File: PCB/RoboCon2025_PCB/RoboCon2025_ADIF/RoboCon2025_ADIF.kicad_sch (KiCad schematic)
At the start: 37 parts, among them J1 Conn_01x05, J2 1x9, J3 Conn_01x09, J4 S2B-XH-A, J5 Micro_SD_Card_Det_Hirose_DM3AT, J6 S3B-XH-A, J7 S2B-XH-A, J8 S2B-XH-A, J9 S3B-XH-A, U1 PCM5102A, U2 MCP23017_SO

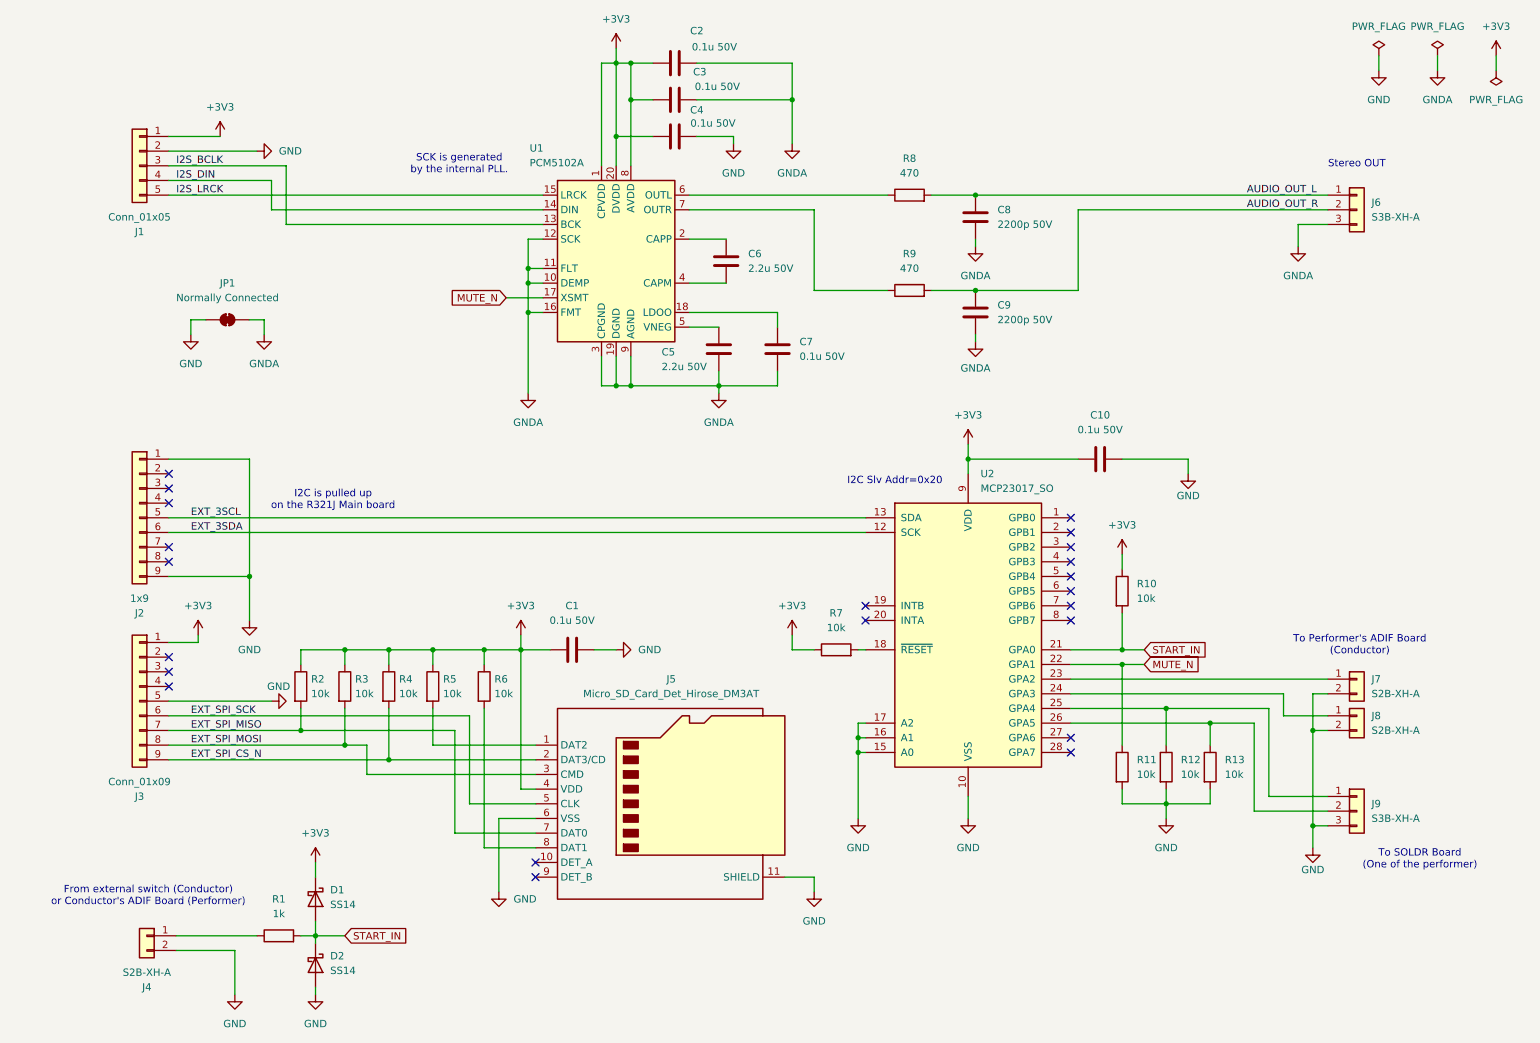
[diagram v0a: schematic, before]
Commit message: [PCB] add: ADIF schematic and layout
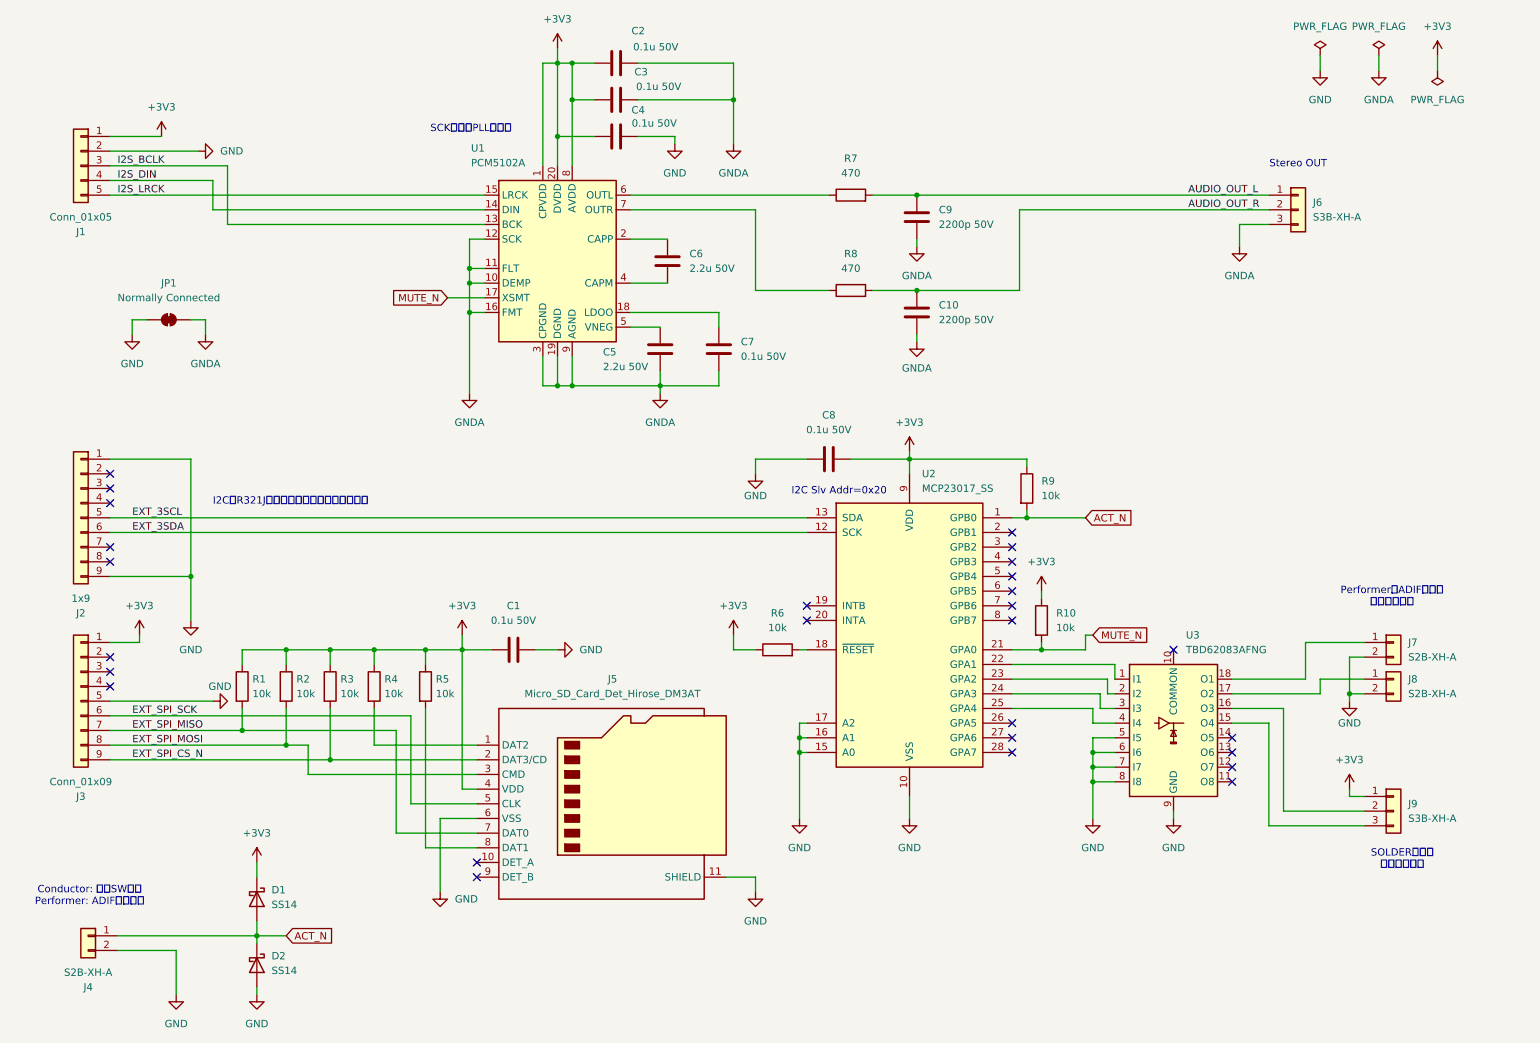
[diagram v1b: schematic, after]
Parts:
- removed R1: 1k, Resistor_SMD:R_0603_1608Metric_Pad0.98x0.95mm_HandSolder, symbol Device:R
- removed R11, R12, R13: 10k, Resistor_SMD:R_0603_1608Metric_Pad0.98x0.95mm_HandSolder, symbol Device:R
- added R10: 10k, Resistor_SMD:R_0603_1608Metric_Pad0.98x0.95mm_HandSolder, symbol Device:R
- added U3: TBD62083AFNG, RoboCon2025_ADIF:TBD62083A_SSOP-18_4.4x6.5mm_P0.65mm, symbol RoboCon2025_ADIF:TBD62083A
- U1: footprint Package_SO:TSSOP-20_4.4x6.5mm_P0.65mm -> Package_SO:Texas_PW0020A_TSSOP-20_4.4x6.5mm_P0.65mm
- U2: value MCP23017_SO -> MCP23017_SS; footprint Package_SO:SOIC-28W_7.5x17.9mm_P1.27mm -> Package_SO:SSOP-28_5.3x10.2mm_P0.65mm
- renumbered C9 to C10, C10 to C8, C8 to C9, R2 to R1, R3 to R2, R4 to R3, R5 to R4, R6 to R5, R7 to R6, R8 to R7, R9 to R8, R10 to R9
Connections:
- net +3V3: now also C8.2, J9.1 (Pin_1), R10.1; no longer C8.1
- net GND: now also C8.1, U3.5 (I5), U3.6 (I6), U3.7 (I7), U3.8 (I8), U3.9 (GND); no longer C8.2, J9.3 (Pin_3)
- net MUTE_N: now also U2.21 (GPA0), R10.2; no longer U2.22 (GPA1)
- net ACT_N: now reaches J4.1 (Pin_1)
- net ACT_N: now also D1.2 (A), D2.1 (K), R9.2, U2.1 (GPB0)
- net at U2.26 (GPA5): no longer J9.2 (Pin_2)
- net at U2.23 (GPA2): now also U3.2 (I2); no longer J7.1 (Pin_1)
- net at U2.24 (GPA3): now also U3.3 (I3); no longer J8.1 (Pin_1)
- net at U2.25 (GPA4): now also U3.4 (I4); no longer J9.1 (Pin_1)
- removed net START_IN: D1.2 (A), D2.1 (K), R9.2, U2.21 (GPA0)
- new net: U2.22 (GPA1), U3.1 (I1)
- new net: J9.2 (Pin_2), U3.16 (O3)
- new net: J9.3 (Pin_3), U3.15 (O4)
- new net: J8.1 (Pin_1), U3.17 (O2)
- new net: J7.1 (Pin_1), U3.18 (O1)
- no-connect marks 22 -> 27
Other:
- note added: "Conductor: 外部SWから Performer: ADIF基板から"
- note added: "I2CはR321Jメインボードでプルアップ済み"
- note added: "PerformerのADIF基板へ 電流吸い込み"
- note added: "SCKは内蔵PLLで生成"
- note added: "SOLDER基板へ 電流吸い込み"
- note removed: "From external switch (Conductor) or Conductor's ADIF Board (Performer)"
- note removed: "I2C is pulled up on the R321J Main board"
- note removed: "SCK is generated by the internal PLL."
- note removed: "To Performer's ADIF Board (Conductor)"
- note removed: "To SOLDR Board (One of the performer)"
- moved on the sheet: C1, C10, C2, C3, C4, C5, C6, C7, C8, C9, D1, D2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

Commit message: ADIF 編集
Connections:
- net AUDIO_OUT_L: now also J6.2 (Pin_2); no longer J6.1 (Pin_1)
- net AUDIO_OUT_R: now also J6.3 (Pin_3); no longer J6.2 (Pin_2)
- net GNDA: now also J6.1 (Pin_1); no longer J6.3 (Pin_3)
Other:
- moved on the sheet: J6
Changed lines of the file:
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@@
 	(wire
 		(pts
+			(xy 236.22 40.64) (xy 236.22 43.18)
+		)
+		(stroke
+			(width 0)
+			(type default)
+		)
+	)
+	(wire
+		(pts
 			(xy 114.3 22.86) (xy 114.3 35.56)
 		)
@@
 	(wire
 		(pts
-			(xy 176.53 45.72) (xy 237.49 45.72)
+			(xy 176.53 45.72) (xy 236.22 45.72)
 		)
 		(stroke
@@
 	(wire
 		(pts
-			(xy 194.31 48.26) (xy 237.49 48.26)
+			(xy 194.31 48.26) (xy 236.22 48.26)
 		)
 		(stroke
@@
 	(wire
 		(pts
-			(xy 232.41 50.8) (xy 232.41 54.61)
-		)
-		(stroke
-			(width 0)
-			(type default)
-		)
-	)
-	(wire
-		(pts
 			(xy 127 68.58) (xy 132.08 68.58)
 		)
@@
 	(wire
 		(pts
+			(xy 233.68 40.64) (xy 236.22 40.64)
+		)
+		(stroke
+			(width 0)
+			(type default)
+		)
+	)
+	(wire
+		(pts
 			(xy 194.31 48.26) (xy 194.31 62.23)
 		)
@@
 	(wire
 		(pts
-			(xy 232.41 50.8) (xy 237.49 50.8)
-		)
-		(stroke
-			(width 0)
-			(type default)
-		)
-	)
-	(wire
-		(pts
 			(xy 41.91 123.19) (xy 36.83 123.19)
 		)
@@
 	(symbol
 		(lib_id "power:GNDA")
-		(at 232.41 54.61 0)
+		(at 233.68 40.64 270)
 		(unit 1)
 		(exclude_from_sim no)
@@
 		(fields_autoplaced yes)
 		(property "Reference" "#PWR030"
-			(at 232.41 60.96 0)
+			(at 227.33 40.64 0)
 			(effects
 				(font
@@
 		)
 		(property "Value" "GNDA"
-			(at 232.41 59.69 0)
+			(at 232.41 36.83 90)
 			(effects
 				(font
@@
 		)
 		(property "Footprint" ""
-			(at 232.41 54.61 0)
+			(at 233.68 40.64 0)
 			(effects
 				(font
@@
 		)
 		(property "Datasheet" ""
-			(at 232.41 54.61 0)
+			(at 233.68 40.64 0)
 			(effects
 				(font
@@
 		)
 		(property "Description" "Power symbol creates a global label with name \"GNDA\" , analog ground"
-			(at 232.41 54.61 0)
+			(at 233.68 40.64 0)
 			(effects
 				(font
@@
 	(symbol
 		(lib_id "Connector_Generic:Conn_01x03")
-		(at 242.57 48.26 0)
+		(at 241.3 45.72 0)
 		(unit 1)
 		(exclude_from_sim no)
@@
 		(fields_autoplaced yes)
 		(property "Reference" "J6"
-			(at 245.11 46.9899 0)
+			(at 243.84 44.4499 0)
 			(effects
 				(font
@@
 		)
 		(property "Value" "S3B-XH-A"
-			(at 245.11 49.5299 0)
+			(at 243.84 46.9899 0)
 			(effects
 				(font
@@
 		)
 		(property "Footprint" "Connector_JST:JST_XH_S3B-XH-A_1x03_P2.50mm_Horizontal"
-			(at 242.57 48.26 0)
+			(at 241.3 45.72 0)
 			(effects
 				(font
@@
 		)
 		(property "Datasheet" "~"
-			(at 242.57 48.26 0)
+			(at 241.3 45.72 0)
 			(effects
 				(font
@@
 		)
 		(property "Description" "Generic connector, single row, 01x03, script generated (kicad-library-utils/schlib/autogen/connector/)"
-			(at 242.57 48.26 0)
+			(at 241.3 45.72 0)
 			(effects
 				(font

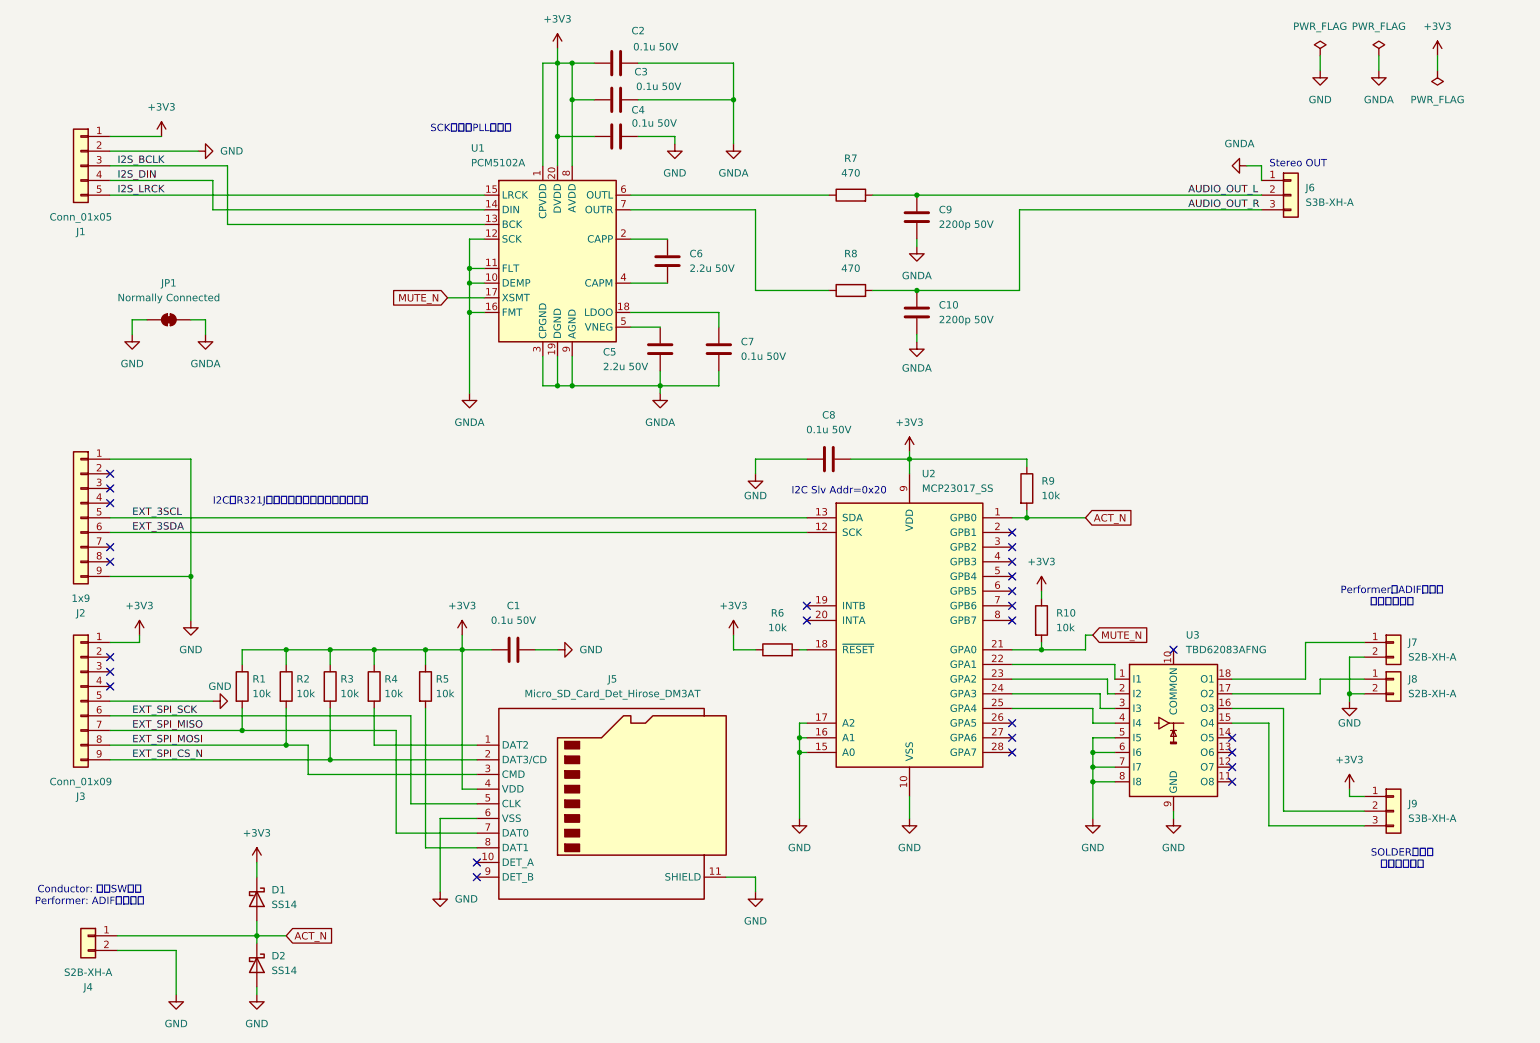
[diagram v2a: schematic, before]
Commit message: [PCB] ADIF基板のIOエキスパンダ部品変更
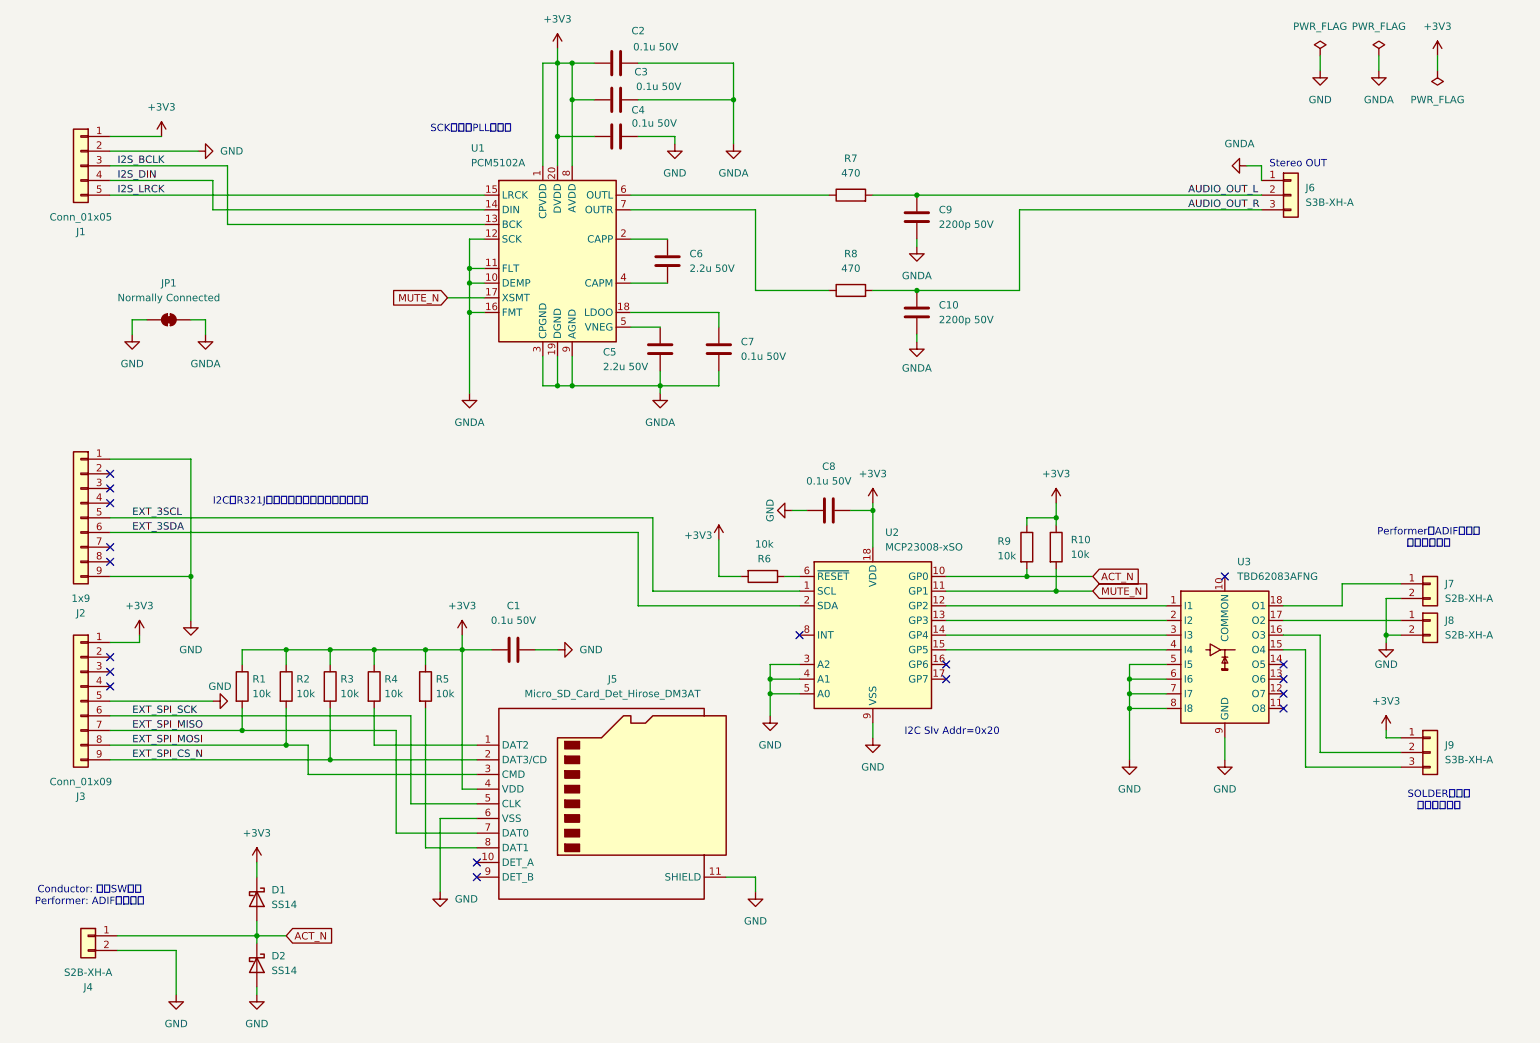
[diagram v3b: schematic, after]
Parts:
- removed U2: MCP23017_SS, Package_SO:SSOP-28_5.3x10.2mm_P0.65mm, symbol Interface_Expansion:MCP23017_SO
- added U2: MCP23008-xSO, Package_SO:SOIC-18W_7.5x11.6mm_P1.27mm, symbol Interface_Expansion:MCP23008-xSO
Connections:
- net +3V3: now also R6.2, U2.18 (VDD); no longer R6.1
- net ACT_N: now also U2.10 (GP0)
- net EXT_3SCL: now also U2.1 (SCL)
- net EXT_3SDA: now also U2.2 (SDA)
- net GND: now also U2.3 (A2), U2.4 (A1), U2.5 (A0), U2.9 (VSS)
- net MUTE_N: now also U2.11 (GP1)
- net at U3.1 (I1): now also U2.12 (GP2)
- net at U3.2 (I2): now also U2.13 (GP3)
- net at U3.3 (I3): now also U2.14 (GP4)
- net at U3.4 (I4): now also U2.15 (GP5)
- new net: R6.1, U2.6 (~{RESET})
- no-connect marks 27 -> 18
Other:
- moved on the sheet: C8, J7, J8, J9, R10, R6, R9, U3

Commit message: [PCB] update: BB基板のパターン引いた(未配線あり)
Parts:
- J1: value Conn_01x05 -> PinSocket_1x5
- J2: value 1x9 -> PinSocket_1x9
- J3: value Conn_01x09 -> PinSocket_1x9
- U2: value MCP23008-xSO -> MCP23008-xSS; footprint Package_SO:SOIC-18W_7.5x11.6mm_P1.27mm -> Package_SO:SSOP-20_5.3x7.2mm_P0.65mm; symbol Interface_Expansion:MCP23008-xSO -> Interface_Expansion:MCP23008-xSS
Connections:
- net +3V3: now also U2.20 (VDD); no longer U2.18 (VDD)
- net ACT_N: now also U2.12 (GP0); no longer U2.10 (GP0)
- net GND: now also C7.2, U1.10 (DEMP), U1.11 (FLT), U1.12 (SCK), U1.16 (FMT), U1.19 (DGND)
- net GNDA: no longer C7.2, U1.10 (DEMP), U1.11 (FLT), U1.12 (SCK), U1.16 (FMT), U1.19 (DGND)
- net MUTE_N: now also U2.13 (GP1); no longer U2.11 (GP1)
- net at U3.1 (I1): now also U2.14 (GP2); no longer U2.12 (GP2)
- net at U3.2 (I2): now also U2.15 (GP3); no longer U2.13 (GP3)
- net at U3.3 (I3): now also U2.16 (GP4); no longer U2.14 (GP4)
- net at U3.4 (I4): now also U2.17 (GP5); no longer U2.15 (GP5)
